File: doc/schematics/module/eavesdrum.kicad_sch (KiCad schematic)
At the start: 96 parts, among them J1 DC37_Pins_MountingHoles, J2 Conn_02x25_Odd_Even, J3 Conn_01x03, SW1 SW_Push, SW2 SW_Push, SW3 SW_Push, U1 CD74HC4067M, U2 CD74HC4067M

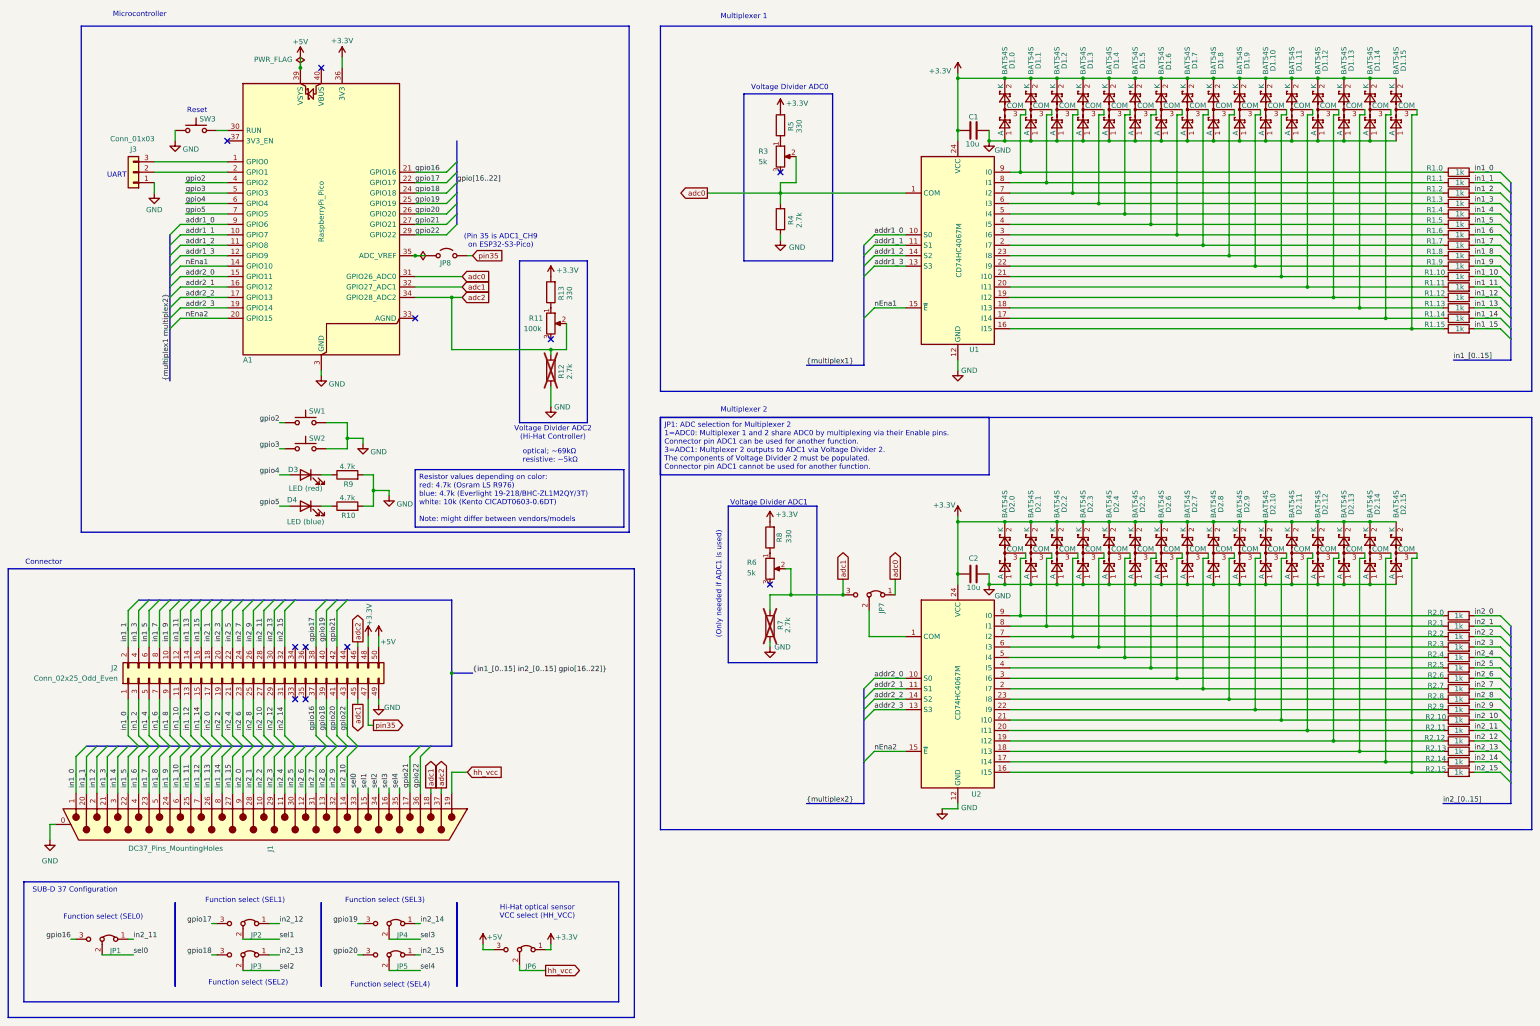
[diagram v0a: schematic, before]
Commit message: module schematic v1.1.1: use header instead of pico
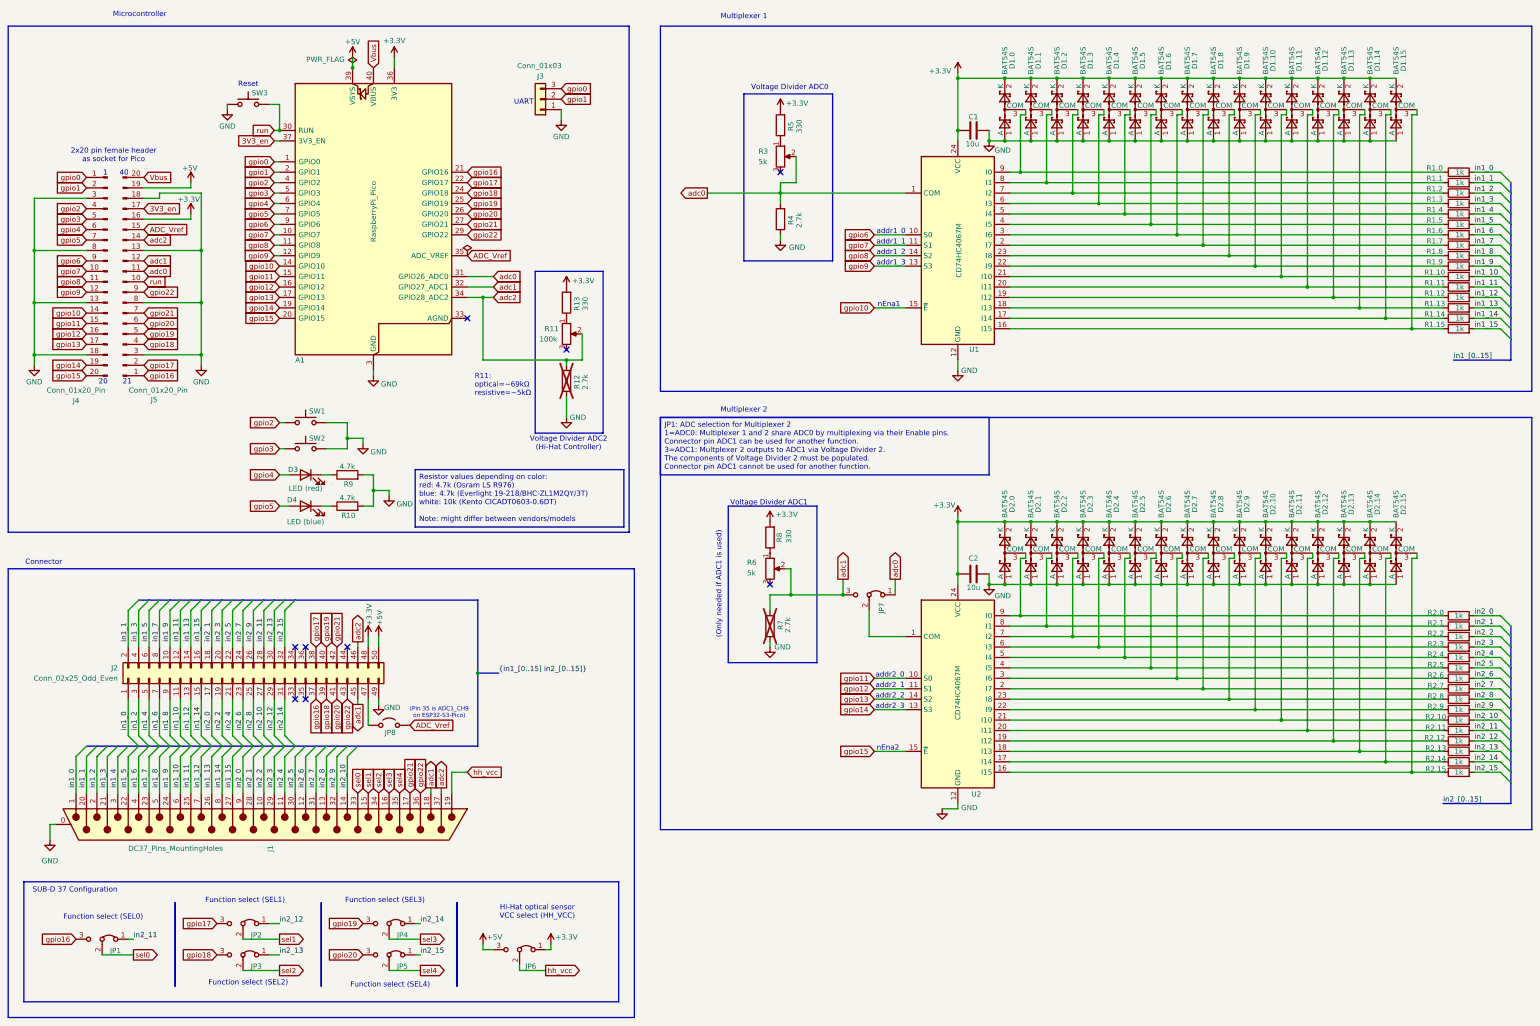
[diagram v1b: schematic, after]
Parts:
- added J4, J5: Conn_01x20_Pin, Connector_PinSocket_2.54mm:PinSocket_1x20_P2.54mm_Vertical, symbol Connector:Conn_01x20_Pin
- J2: footprint Connector_IDC:IDC-Header_2x25_P2.54mm_Vertical_SMD -> Connector_IDC:IDC-Header_2x25_P2.54mm_Vertical
- R11, R3, R6: footprint Potentiometer_SMD:Potentiometer_Bourns_TC33X_Vertical -> Potentiometer_SMD:Potentiometer_ACP_CA9-VSMD_Vertical
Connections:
- net +3.3V: now also J5.16 (Pin_16)
- net +5V: now also J5.19 (Pin_19)
- net GND: now also J4.13 (Pin_13), J4.18 (Pin_18), J4.3 (Pin_3), J4.8 (Pin_8), J5.13 (Pin_13), J5.18 (Pin_18), J5.3 (Pin_3), J5.8 (Pin_8)
- net adc0: now also J5.11 (Pin_11)
- net adc1: now also J5.12 (Pin_12)
- net adc2: now also J5.14 (Pin_14)
- net gpio16: now also J5.1 (Pin_1)
- net gpio17: now also J5.2 (Pin_2)
- net gpio18: now also J5.4 (Pin_4)
- net gpio19: now also J5.5 (Pin_5)
- net gpio2: now also J4.4 (Pin_4)
- net gpio20: now also J5.6 (Pin_6)
- net gpio21: now also J5.7 (Pin_7)
- net gpio22: now also J5.9 (Pin_9)
- net gpio3: now also J4.5 (Pin_5)
- net gpio4: now also J4.6 (Pin_6)
- net gpio5: now also J4.7 (Pin_7)
- net ADC_Vref: now reaches A1.35 (ADC_VREF), JP8.1 (A)
- net ADC_Vref: now also J5.15 (Pin_15)
- net gpio1: now reaches A1.2 (GPIO1), J3.2 (Pin_2)
- net gpio1: now also J4.2 (Pin_2)
- net gpio0: now reaches A1.1 (GPIO0), J3.3 (Pin_3)
- net gpio0: now also J4.1 (Pin_1)
- net run: now reaches A1.30 (RUN), SW3.2
- net run: now also J5.10 (Pin_10)
- net 3V3_en: now reaches A1.37 (3V3_EN)
- net 3V3_en: now also J5.17 (Pin_17)
- net Vbus: now reaches A1.40 (VBUS)
- net Vbus: now also J5.20 (Pin_20)
- net addr1_0 renamed gpio6
- net gpio6: now also J4.9 (Pin_9)
- net addr1_1 renamed gpio7
- net gpio7: now also J4.10 (Pin_10)
- net addr1_2 renamed gpio8
- net gpio8: now also J4.11 (Pin_11)
- net addr1_3 renamed gpio9
- net gpio9: now also J4.12 (Pin_12)
- net addr2_0 renamed gpio11
- net gpio11: now also J4.15 (Pin_15)
- net addr2_1 renamed gpio12
- net gpio12: now also J4.16 (Pin_16)
- net addr2_2 renamed gpio13
- net gpio13: now also J4.17 (Pin_17)
- net addr2_3 renamed gpio14
- net gpio14: now also J4.19 (Pin_19)
- net nEna1 renamed gpio10
- net gpio10: now also J4.14 (Pin_14)
- net nEna2 renamed gpio15
- net gpio15: now also J4.20 (Pin_20)
- net pin35: no longer names the net of J2.47 (Pin_47), JP8.2 (B)
- no-connect marks 11 -> 9
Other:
- note added: "1"
- note added: "20"
- note added: "21"
- note added: "2x20 pin female header as socket for Pico"
- note added: "40"
- note added: "R11: optical=~69kΩ resistive=~5kΩ"
- note added: "addr1_0"
- note added: "addr1_1"
- note added: "addr1_2"
- note added: "addr1_3"
- note added: "addr2_0"
- note added: "addr2_1"
- note added: "addr2_2"
- note added: "addr2_3"
- note added: "nEna1"
- note added: "nEna2"
- note removed: "optical; ~69kΩ resistive: ~5kΩ"
- moved on the sheet: A1, J3, JP8, R11, R12, R13, SW3
